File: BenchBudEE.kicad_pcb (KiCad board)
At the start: 4 copper layers, 165.1 x 63.5 mm, 0 parts

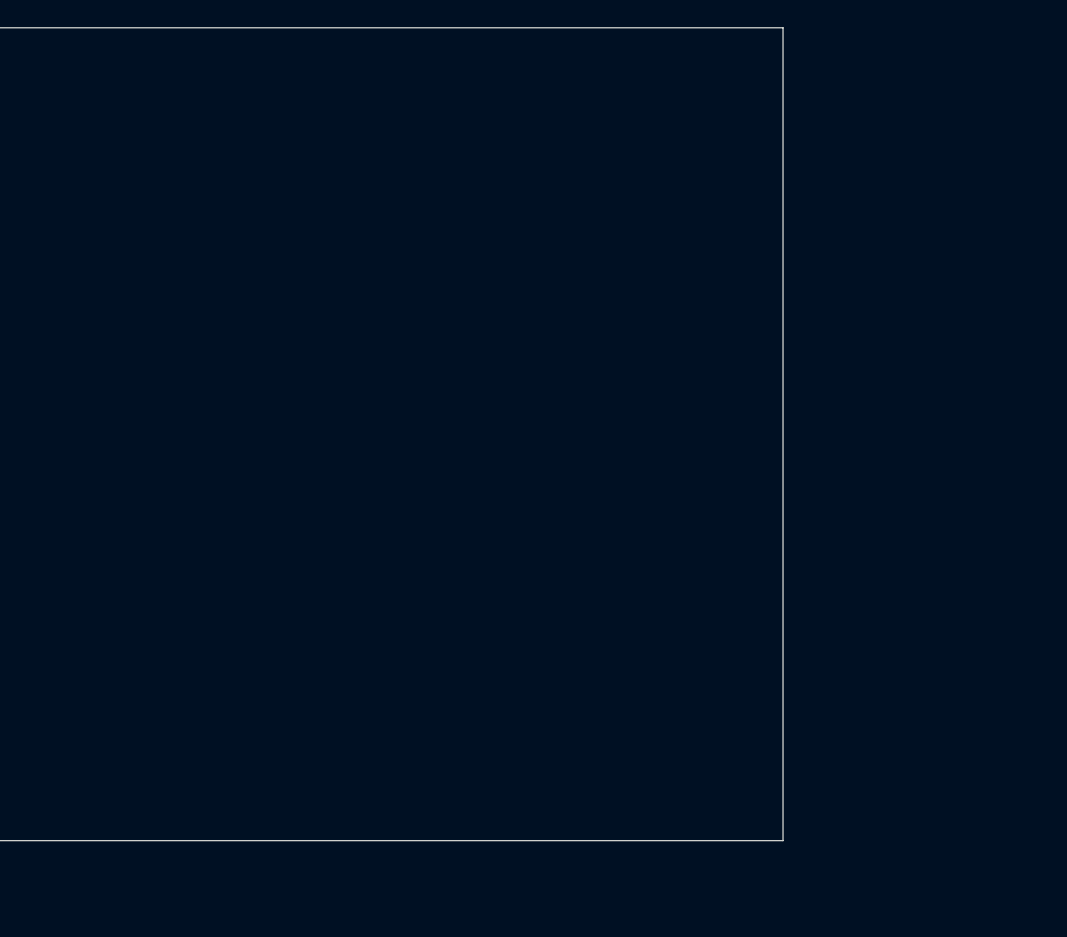
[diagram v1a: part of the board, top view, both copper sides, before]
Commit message: worked on associating parts
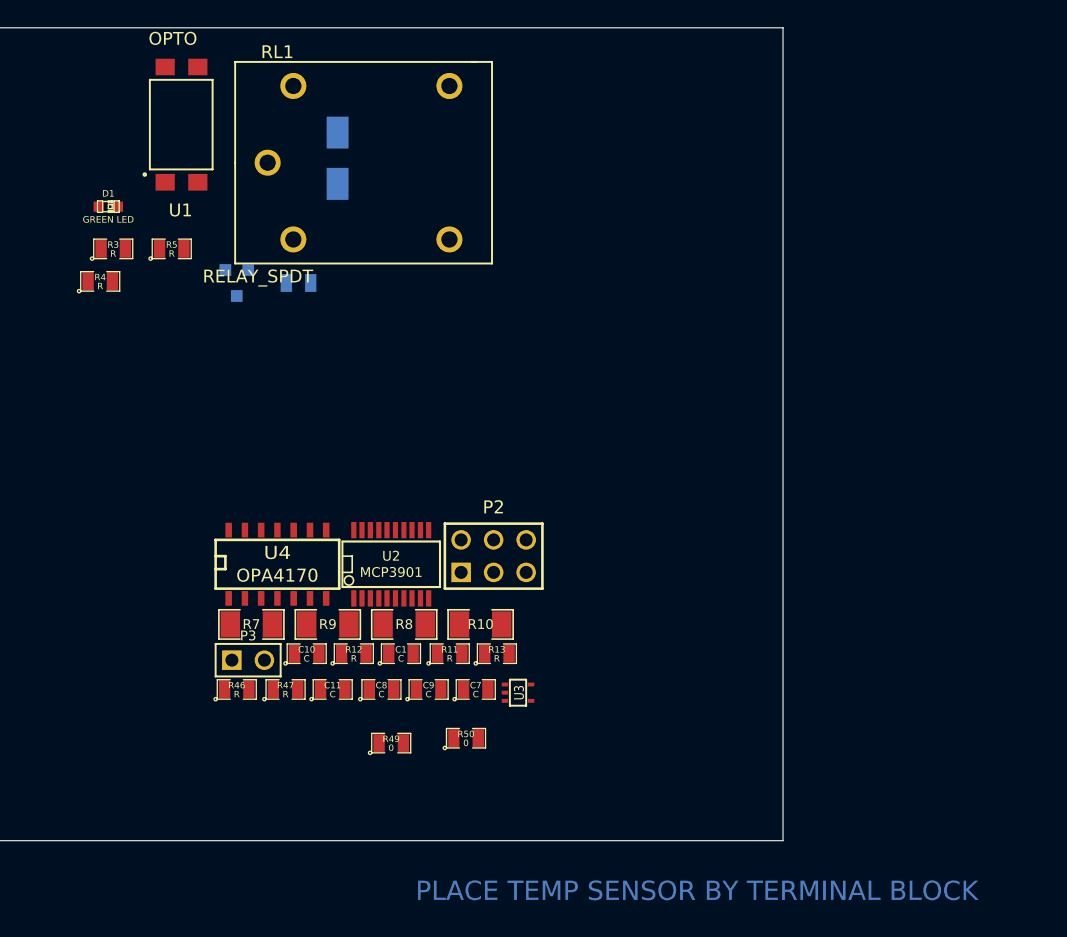
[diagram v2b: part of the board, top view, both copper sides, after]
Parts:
- added C1: C, SM0805, F.Cu at (275.6, 168.0)
- added C10: C, SM0805, F.Cu at (268.2, 168.0)
- added C11: C, SM0805, F.Cu at (270.3, 170.8)
- added C7: C, SM0805, F.Cu at (281.4, 170.8)
- added C8: C, SM0805, F.Cu at (274.1, 170.8)
- added C9: C, SM0805, F.Cu at (277.7, 170.8)
- added D1: GREEN LED, LED-0603, F.Cu at (252.7, 133.1)
- added D2: DIODE, SMA-DIODE, B.Cu at (270.6, 131.3)
- added P2: CONN_3X2, pin_array_3x2, F.Cu at (282.8, 160.4)
- added P3: CONN_2, PIN_ARRAY_2X1, F.Cu at (263.7, 168.5)
- added Q1: NPN, SOT23EBC, B.Cu at (262.8, 139.1)
- added R10: R, SM1206, F.Cu at (281.8, 165.7)
- added R11: R, SM0805, F.Cu at (279.4, 168.0)
- added R12: R, SM0805, F.Cu at (271.9, 168.0)
- added R13: R, SM0805, F.Cu at (283.1, 168.0)
- added R3: R, SM0805, F.Cu at (253.1, 136.4)
- added R4: R, SM0805, F.Cu at (252.1, 138.9)
- added R46: R, SM0805, F.Cu at (262.8, 170.8)
- added R47: R, SM0805, F.Cu at (266.6, 170.8)
- added R49: 0, SM0805, F.Cu at (274.8, 175.0)
- added R5: R, SM0805, F.Cu at (257.7, 136.4)
- added R50: 0, SM0805, F.Cu at (280.7, 174.6)
- added R6: R, SM0805, B.Cu at (267.6, 139.1)
- added R7: R, SM1206, F.Cu at (263.9, 165.7)
- added R8: R, SM1206, F.Cu at (275.8, 165.7)
- added R9: R, SM1206, F.Cu at (269.9, 165.7)
- added RL1: RELAY_SPDT, TE_SPDT, F.Cu at (265.2, 129.7)
- added U1: OPTO, 4-SMD, F.Cu at (257.2, 131.2)
- added U2: MCP3901, SSOP20, F.Cu at (274.8, 161.0)
- added U3: LMT84, SOT353, F.Cu at (284.7, 171.1)
- added U4: OPA4170, SO14E, F.Cu at (265.9, 160.9)
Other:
- board text added: "PLACE TEMP SENSOR BY TERMINAL BLOCK"

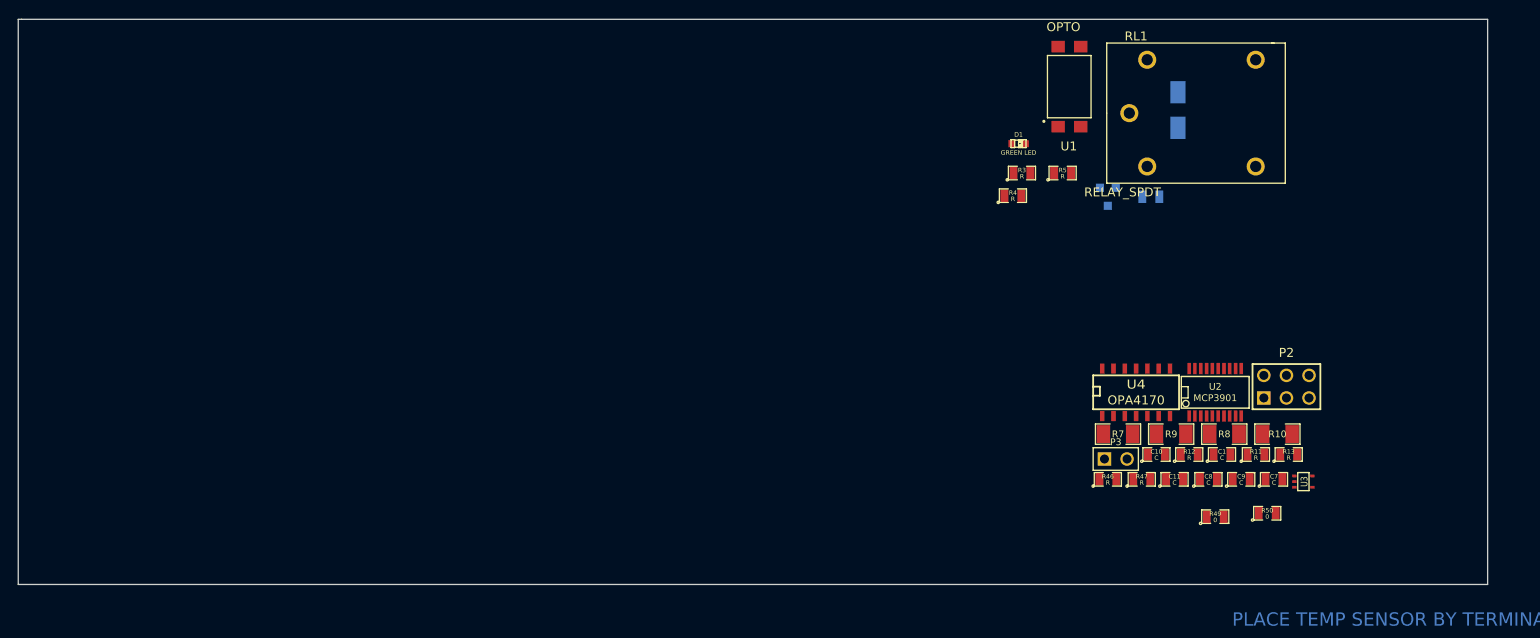
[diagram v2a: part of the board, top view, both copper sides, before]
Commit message: Completed terminal block placement and footprints
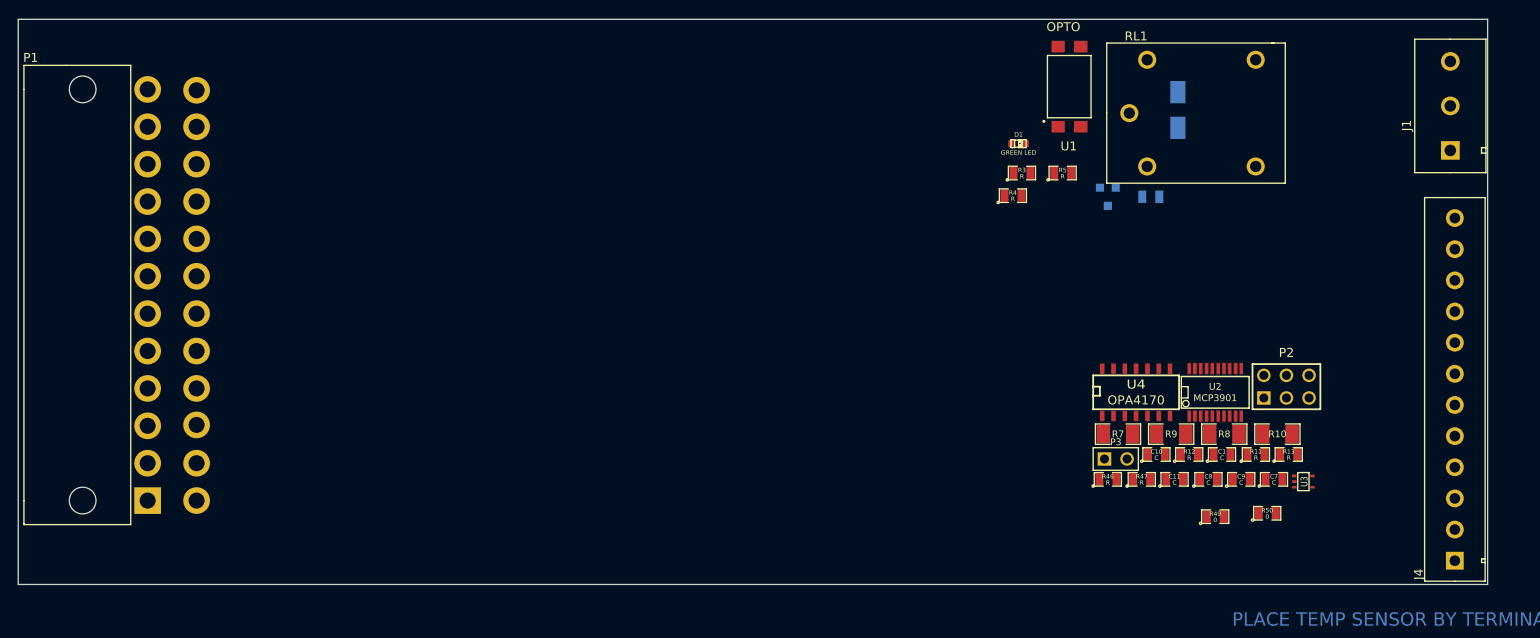
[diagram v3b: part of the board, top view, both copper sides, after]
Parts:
- added J1: 3 Pin TB, 3pinTermBlock, F.Cu at (301.2, 133.9)
- added J4: 12 Pin Terminal Block, 12pinTermBlock, F.Cu at (301.8, 180.0)
- added P1: 24 Pin ATX, ATX_Header, F.Cu at (147.6, 127.0)
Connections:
- RL1 pad 1: (no net) -> /Relay/RELAY_COM
- RL1 pad 3: (no net) -> /Relay/RELAY_NO
- RL1 pad 4: (no net) -> /Relay/RELAY_NC

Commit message: Completed Arduino footprint and association
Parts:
- added ARD1: ARDUINOPINS, Arduino, F.Cu at (209.0, 177.3)
- added R27: R, RES_SM0805, F.Cu at (178.3, 170.4)
- added R28: R, RES_SM0805, F.Cu at (180.8, 170.4)
- added R29: R, RES_SM0805, F.Cu at (183.4, 170.4)
- added R30: R, RES_SM0805, F.Cu at (185.9, 170.4)
- added R31: R, RES_SM0805, F.Cu at (191.0, 170.4)
- added R32: R, RES_SM0805, F.Cu at (193.5, 170.4)
- added R33: R, RES_SM0805, F.Cu at (196.1, 170.4)
- added R34: R, RES_SM0805, F.Cu at (198.6, 170.4)
- added R35: R, RES_SM0805, F.Cu at (168.9, 129.5)
- added R36: R, RES_SM0805, F.Cu at (171.7, 130.0)
- added R37: R, RES_SM0805, F.Cu at (174.5, 130.3)
- added R38: R, RES_SM0805, F.Cu at (177.0, 130.3)
- added R39: R, RES_SM0805, F.Cu at (179.6, 130.0)
- added R40: R, RES_SM0805, F.Cu at (182.1, 130.3)
- added R41: R, RES_SM0805, F.Cu at (185.9, 130.3)
- added R42: R, RES_SM0805, F.Cu at (201.4, 130.0)
- added R43: R, RES_SM0805, F.Cu at (204.2, 130.0)
- added R44: R, RES_SM0805, F.Cu at (212.9, 163.6)
- added R45: R, RES_SM0805, F.Cu at (191.3, 130.3)
- moved P1 0.57 mm to (147.1, 127.3)
